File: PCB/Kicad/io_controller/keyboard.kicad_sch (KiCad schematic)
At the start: 1 part, among them U33 74LS377

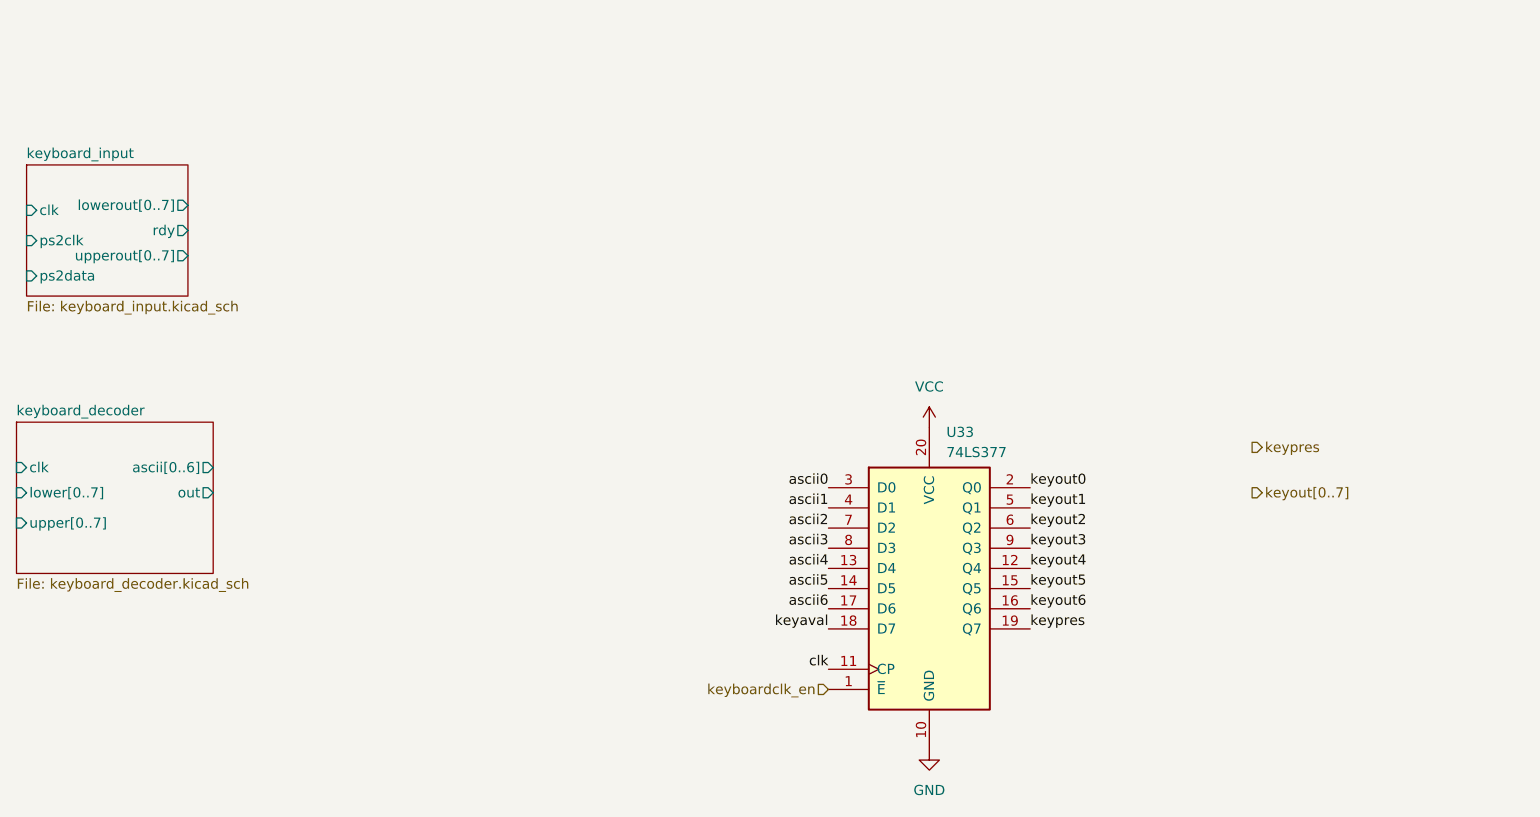
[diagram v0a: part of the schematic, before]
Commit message: initial version of io controller schematic
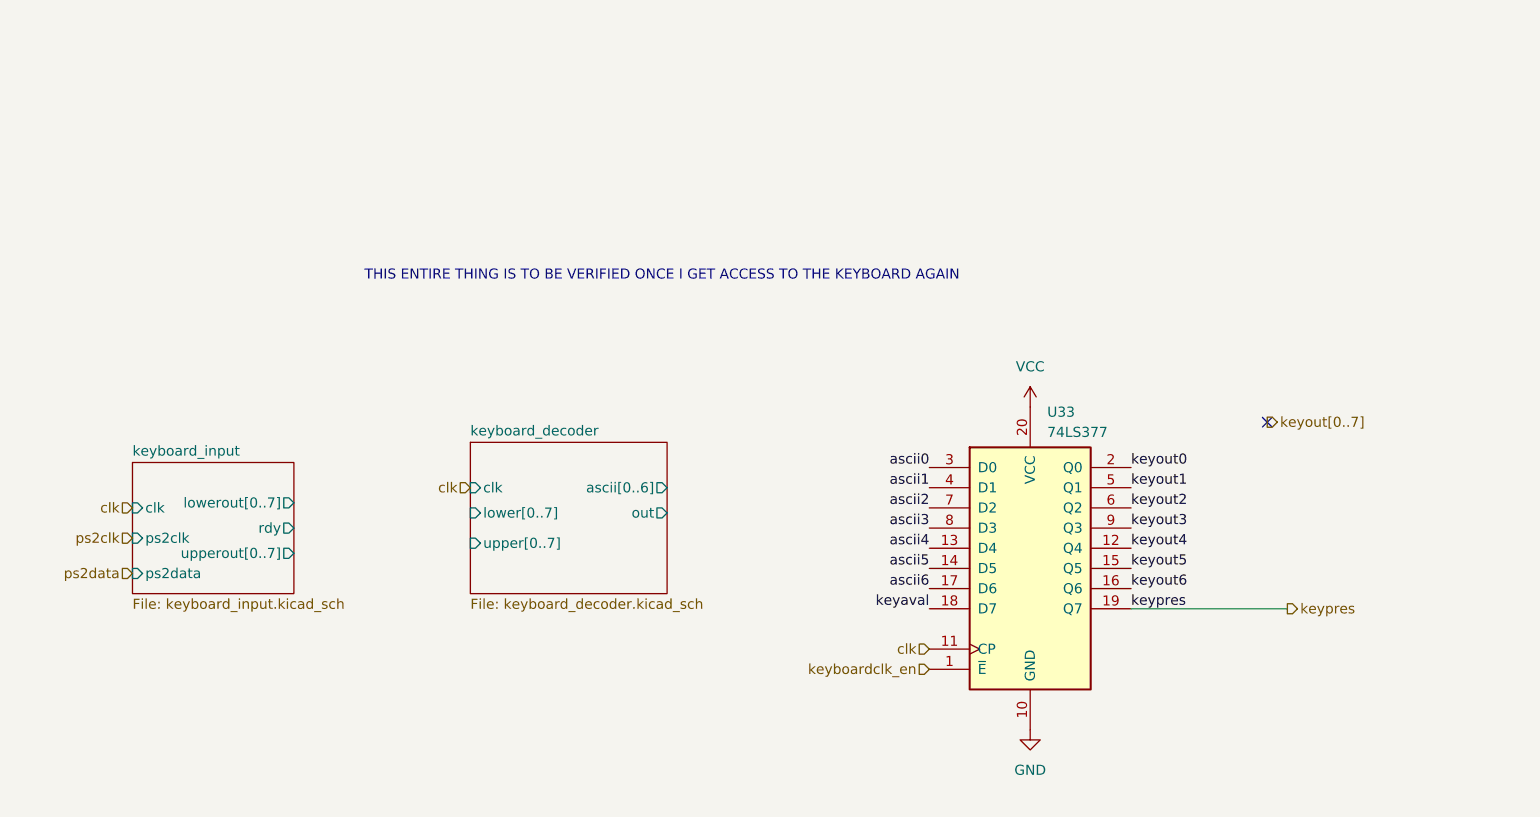
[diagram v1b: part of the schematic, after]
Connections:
- no-connect marks 0 -> 1
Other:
- note added: "THIS ENTIRE THING IS TO BE VERIFIED ONCE I GET ACCESS TO THE KEYBOARD AGAIN"
- moved on the sheet: U33

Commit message: more spice models and bugfixes ; more tests of io_controller - mostly keyboard
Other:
- sheet keyboard_decoder ports: added rdy, ~{rst}; removed none
- sheet keyboard_input ports: added rdyout, ~{rst}; removed rdy

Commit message: primarily keyboard decoder finish ; preliminary layout
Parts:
- removed U33: 74LS377, symbol 74xx:74LS377
- added Ck1, Ck2: 0.1u, Capacitor_SMD:C_0402_1005Metric, symbol Device:C
- added Uk1: 74LS377, Package_SO:SSOP-20_5.3x7.2mm_P0.65mm, symbol 74xx:74LS377
- added Uk2: 74LS02, Package_SO:SOIC-14_3.9x8.7mm_P1.27mm, symbol 74xx:74LS02
- added Uki5: 74LS08, Package_SO:SOIC-14_3.9x8.7mm_P1.27mm, symbol 74xx:74LS08
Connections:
- net GND: now also Ck1.2, Ck2.2, Uk1.1 (~{E}), Uk1.10 (GND), Uk2.7 (GND)
- net VCC: now also Ck1.1, Ck2.1, Uk1.14 (D5), Uk1.17 (D6), Uk1.18 (D7), Uk1.20 (VCC), Uk2.11, Uk2.12, Uk2.14 (VCC)
- net clk: now also Uk1.11 (CP)
- net ~{rst}: now also Uki5.12
- new net: Uk2.4, Uki5.5
- new net: Uk2.10, Uk2.5, Uk2.6
- new net: Uki5.13, Uki5.6
- new net: Uk2.1, Uki5.4
- new net: Uk1.13 (D4), Uk1.9 (Q3)
- new net: Uk1.2 (Q0), Uk1.4 (D1)
- new net: Uk1.6 (Q2), Uk1.8 (D3)
- new net keyready: Uk2.9, Uki5.11
- new net newkey: Uk1.7 (D2)
- new net read: Uk1.3 (D0)
- new net reset: Uk1.12 (Q4), Uk2.8
- new net set: Uk1.5 (Q1), Uk2.2, Uk2.3
- no-connect marks 1 -> 5
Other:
- note added: "SR latch with priority for release"
- note removed: "THIS ENTIRE THING IS TO BE VERIFIED ONCE I GET ACCESS TO THE KEYBOARD AGAIN"
- company: (none) -> AGH Logic Unit
- title: (none) -> Keyboard Controller

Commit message: io controller update
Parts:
- Ck1, Ck2: value 0.1u -> 100nF
- Uk1: value 74LS377 -> 74377
- Uk2: value 74LS02 -> 7402
- Uki5: value 74LS08 -> 7408; footprint Package_SO:SOIC-14_3.9x8.7mm_P1.27mm -> Package_SO:SO-14_3.9x8.65mm_P1.27mm
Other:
- note removed: "figure out what these outputs are"

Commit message: Forgot to add few things
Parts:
- Uk2: footprint Package_SO:SOIC-14_3.9x8.7mm_P1.27mm -> Package_SO:SO-14_3.9x8.65mm_P1.27mm
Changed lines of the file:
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@@
 			)
 		)
-		(property "Footprint" "Package_SO:SOIC-14_3.9x8.7mm_P1.27mm"
+		(property "Footprint" "Package_SO:SO-14_3.9x8.65mm_P1.27mm"
 			(at 75.565 132.715 0)
 			(hide yes)
@@
 			)
 		)
-		(property "Datasheet" "http://www.ti.com/lit/gpn/sn74ls02"
+		(property "Datasheet" "https://www.tme.eu/pl/en/details/sn74hc02dr/gates-inverters/texas-instruments/"
 			(at 75.565 132.715 0)
 			(hide yes)
@@
 			)
 		)
-		(property "Footprint" "Package_SO:SOIC-14_3.9x8.7mm_P1.27mm"
+		(property "Footprint" "Package_SO:SO-14_3.9x8.65mm_P1.27mm"
 			(at 56.515 147.955 0)
 			(hide yes)
@@
 			)
 		)
-		(property "Datasheet" "http://www.ti.com/lit/gpn/sn74ls02"
+		(property "Datasheet" "https://www.tme.eu/pl/en/details/sn74hc02dr/gates-inverters/texas-instruments/"
 			(at 56.515 147.955 0)
 			(hide yes)
@@
 			)
 		)
-		(property "Footprint" "Package_SO:SOIC-14_3.9x8.7mm_P1.27mm"
+		(property "Footprint" "Package_SO:SO-14_3.9x8.65mm_P1.27mm"
 			(at 207.645 95.885 0)
 			(hide yes)
@@
 			)
 		)
-		(property "Description" "quad 2-input NOR gate"
+		(property "Description" "https://www.tme.eu/pl/en/details/sn74hc02dr/gates-inverters/texas-instruments/"
 			(at 207.645 95.885 0)
 			(hide yes)
@@
 			)
 		)
-		(property "Footprint" "Package_SO:SOIC-14_3.9x8.7mm_P1.27mm"
+		(property "Footprint" "Package_SO:SO-14_3.9x8.65mm_P1.27mm"
 			(at 77.47 116.84 0)
 			(hide yes)
@@
 			)
 		)
-		(property "Datasheet" "http://www.ti.com/lit/gpn/sn74ls02"
+		(property "Datasheet" "https://www.tme.eu/pl/en/details/sn74hc02dr/gates-inverters/texas-instruments/"
 			(at 77.47 116.84 0)
 			(hide yes)
@@
 			)
 		)
-		(property "Footprint" "Package_SO:SOIC-14_3.9x8.7mm_P1.27mm"
+		(property "Footprint" "Package_SO:SO-14_3.9x8.65mm_P1.27mm"
 			(at 210.82 123.19 0)
 			(hide yes)
@@
 			)
 		)
-		(property "Datasheet" "http://www.ti.com/lit/gpn/sn74ls02"
+		(property "Datasheet" "https://www.tme.eu/pl/en/details/sn74hc02dr/gates-inverters/texas-instruments/"
 			(at 210.82 123.19 0)
 			(hide yes)
@@
 			)
 		)
-		(property "Description" "quad 2-input NOR gate"
+		(property "Description" "https://www.tme.eu/pl/en/details/sn74hc02dr/gates-inverters/texas-instruments/"
 			(at 210.82 123.19 0)
 			(hide yes)
